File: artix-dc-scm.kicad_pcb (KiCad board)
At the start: 8 copper layers, 90 x 120.4 mm, 474 parts, among them IC1 TPS54561, IC2 TLV73312PDBVT, J1 L834-1G1T-S7, J12 S2B-PH-K-S_LF__SN_, J13 62000311121, J2 1-2199230-6, J3 543630489, J4 M20-7830642, J5 SFF-TA-1002-4C+, J6 0878311420, J7 61300611121, Q1 IRLML6402TRPBF, Q10 2N7002, Q11 2N7002, Q12 2N7002, Q13 2N7002, Q14 2N7002, Q15 2N7002, Q16 2N7002, Q2 IRLML6402TRPBF, Q3 IRLML6402TRPBF, Q4 IRLML6402TRPBF, Q5 IRLML6402TRPBF, Q6 IRLML6402TRPBF, Q7 2N7002, Q8 2N7002, Q9 2N7002, U1 MTFC16GAPALNA-AIT, U10 TPS62823DLCT, U11 TPS62823DLCT, U12 TPS62823DLCT, U13 TPS62823DLCT, U14 XC7A100T-FGG484, U15 SN74LVC1G08DCKR, U16 SN74LS08DBR, U17 USB3300-EZK-TR, U18 USB3300-EZK-TR, U2 W25Q32JVSSIQ_TR, U20 KSZ9031RNXCA, U3 W25Q32JVSSIQ_TR, U4 W25Q32JVSSIQ_TR, U5 W25Q32JVSSIQ_TR, U6 NVT2008DQ,115, U7 AS4C256M16D3, U8 TPS51200DRC, U9 LM3881MME_NOPB, Y1 TSX-3225, Y2 ABM8G-25.000MHZ-18-D2Y-T, Y3 TSX-3225

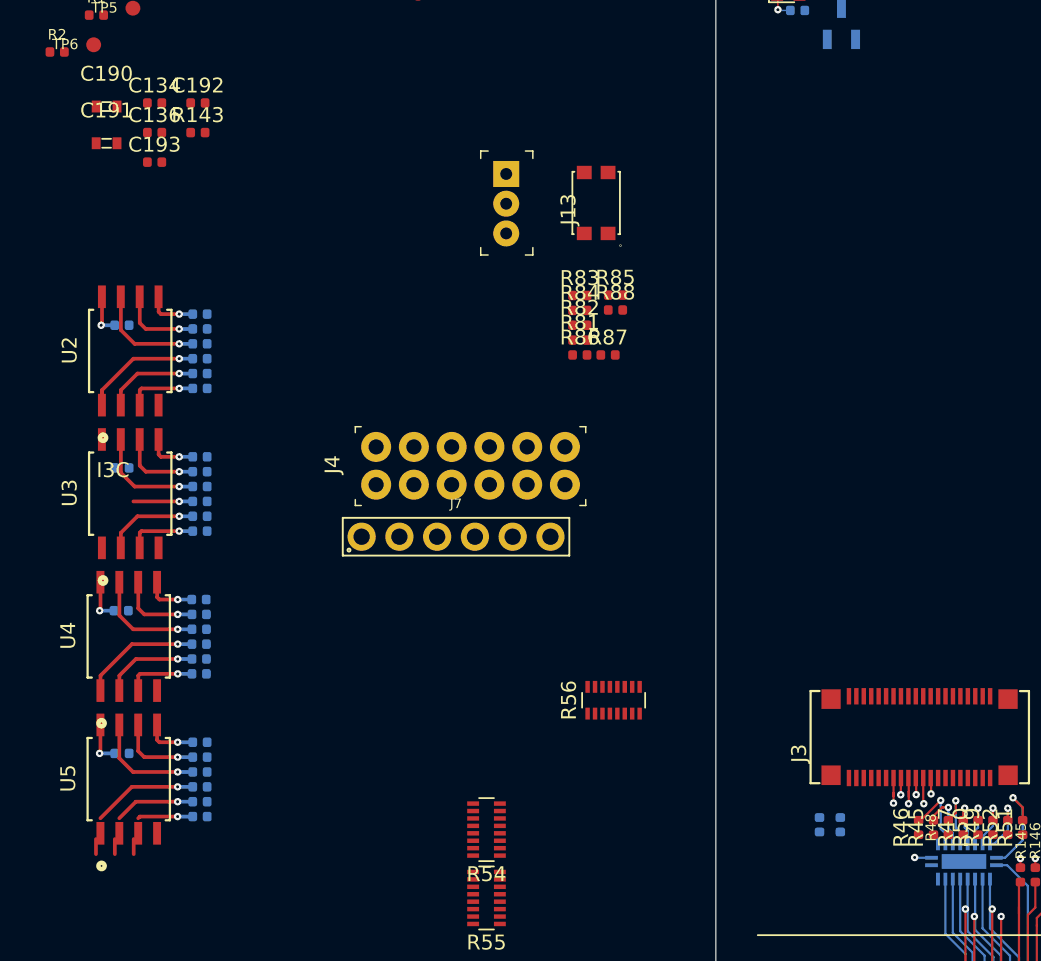
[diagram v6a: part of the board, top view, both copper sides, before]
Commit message: move Flash ICs under RoT
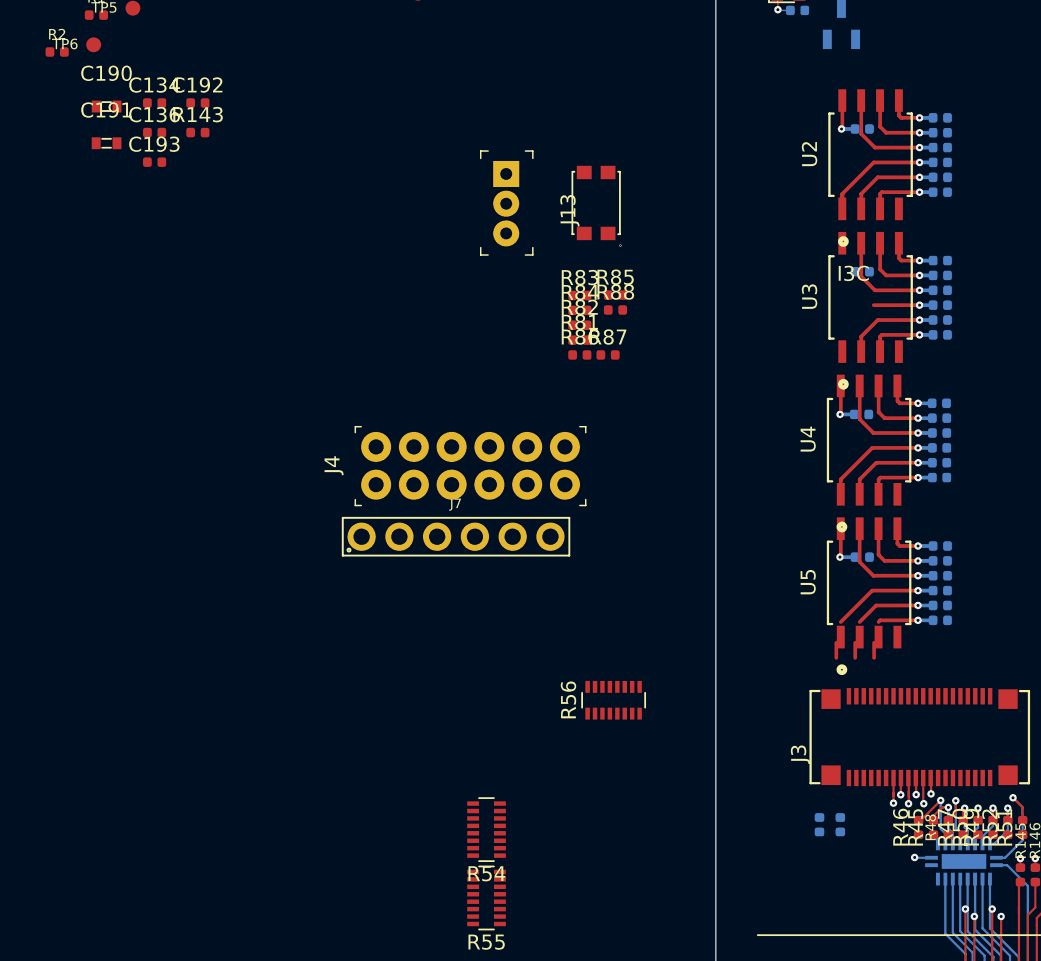
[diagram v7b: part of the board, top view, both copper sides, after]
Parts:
- moved C35 51.5 mm to (70.0, 115.1)
- moved C36 51.5 mm to (70.0, 124.7)
- moved R21 51.5 mm to (75.2, 117.3)
- moved R22 51.5 mm to (75.2, 126.9)
- moved R25 51.5 mm to (75.2, 115.3)
- moved R26 51.5 mm to (75.2, 124.9)
- moved R29 51.5 mm to (75.2, 114.3)
- moved R30 51.5 mm to (75.2, 123.9)
- moved R33 51.5 mm to (75.2, 119.3)
- moved R37 51.5 mm to (75.2, 116.3)
- moved R38 51.5 mm to (75.2, 125.9)
- moved R41 51.5 mm to (75.2, 118.3)
- moved R42 51.5 mm to (75.2, 127.9)
- moved U4 51.5 mm to (70.4, 136.0)
- moved U5 51.5 mm to (70.4, 145.6)
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
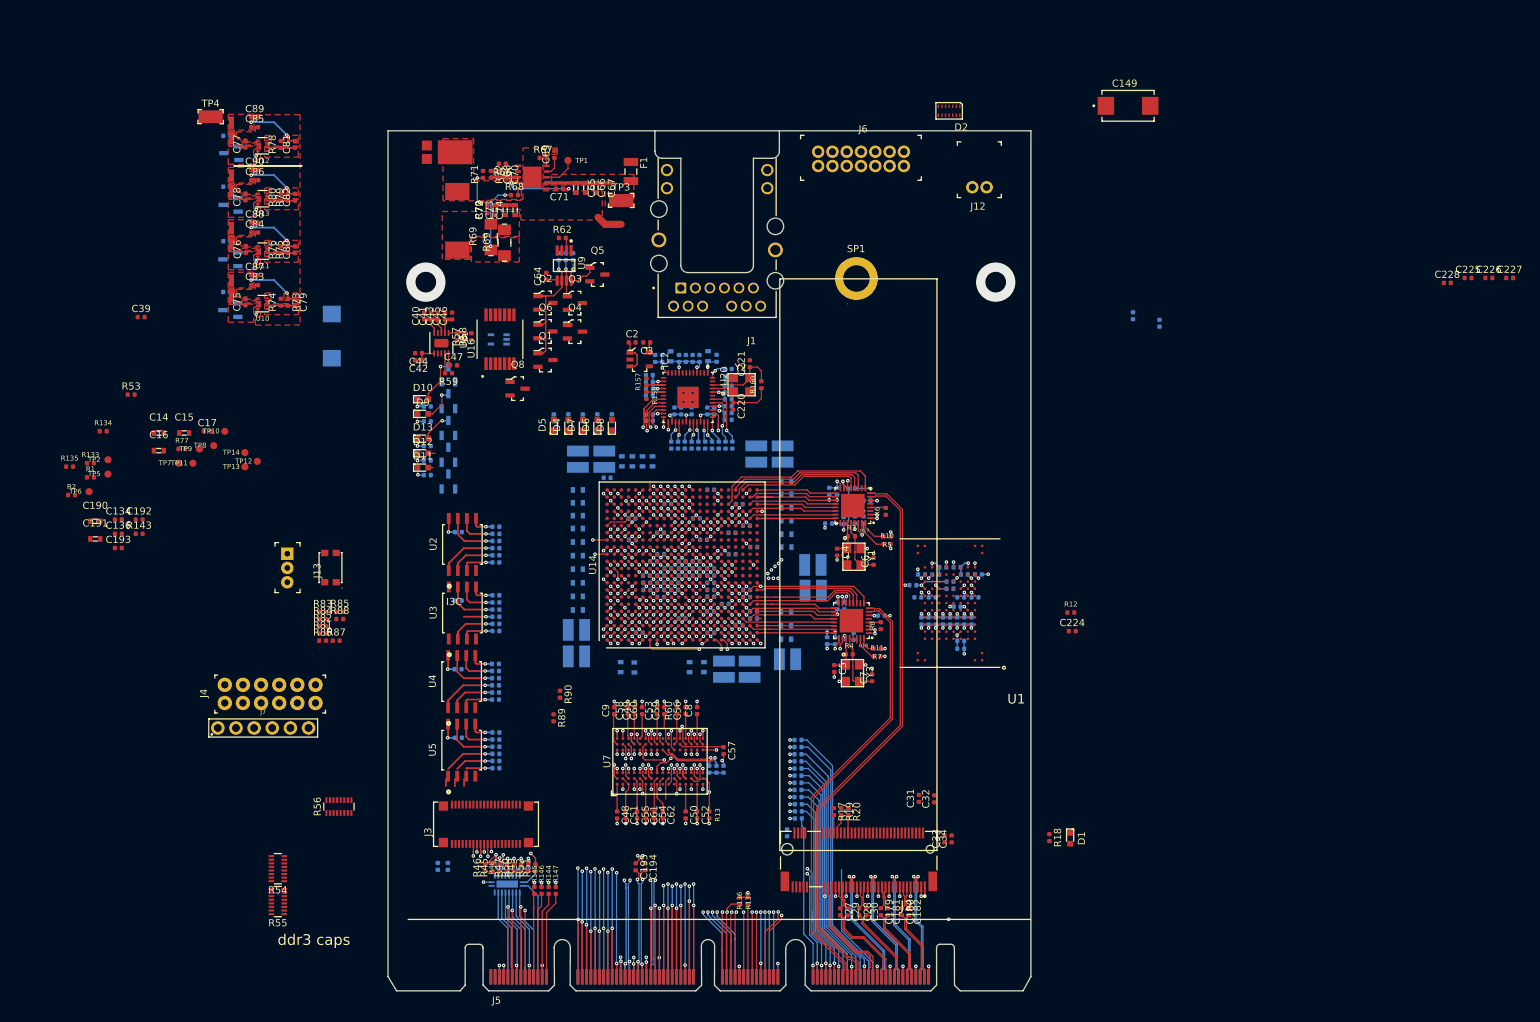
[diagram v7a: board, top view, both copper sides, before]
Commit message: Fix PCB outline
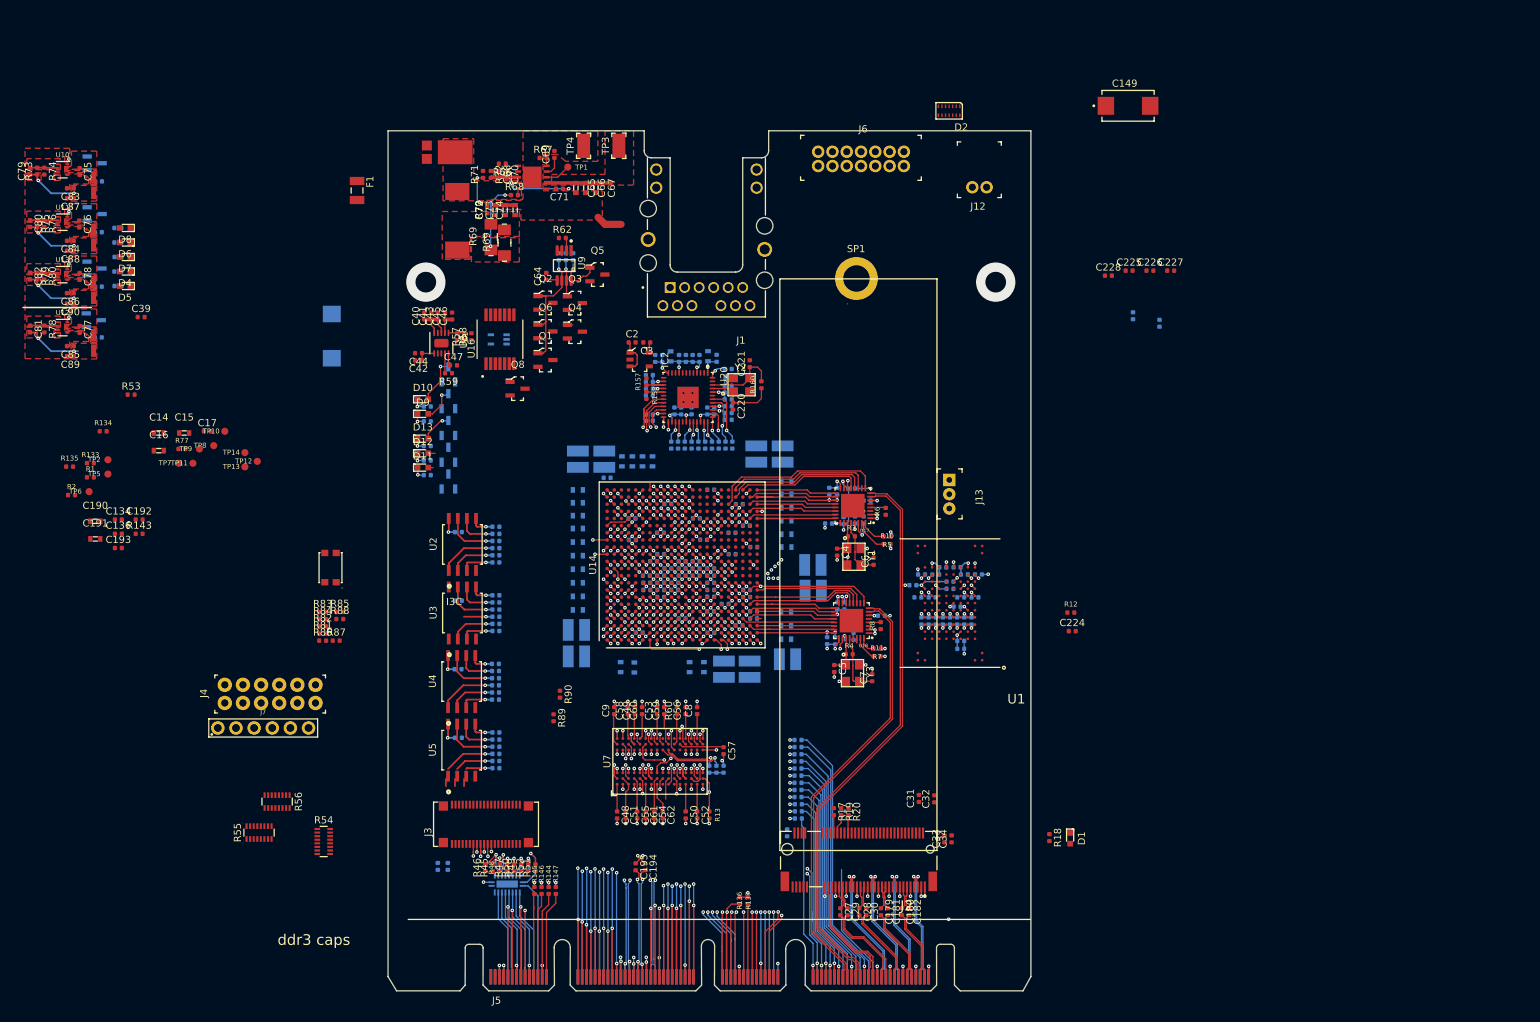
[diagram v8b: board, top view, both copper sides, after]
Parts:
- moved J13 93.2 mm to (138.7, 109.8)
- moved R98 74.1 mm to (22.3, 72.5), turned to 0 degrees
- moved D8 73.5 mm to (23.3, 72.5), turned to 180 degrees
- moved R96 71.5 mm to (22.3, 74.5), turned to 0 degrees
- moved D6 70.9 mm to (23.3, 74.5), turned to 180 degrees
- moved R97 68.9 mm to (22.3, 76.6), turned to 0 degrees
- moved D7 68.3 mm to (23.3, 76.6), turned to 180 degrees
- moved R94 66.3 mm to (22.3, 78.6), turned to 0 degrees
- moved D4 65.7 mm to (23.3, 78.6), turned to 180 degrees
- moved R95 63.7 mm to (22.3, 80.6), turned to 0 degrees
- moved D5 63.1 mm to (23.3, 80.6), turned to 180 degrees
- moved TP4 52.4 mm to (87.5, 61.0), turned to 90 degrees
- moved C225 47.5 mm to (163.8, 78.5)
- moved C226 47.5 mm to (166.8, 78.5)
- moved C227 47.5 mm to (169.7, 78.5)
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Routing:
- net Net-(IC1-Pad3): track 4.64 -> 3.57 mm
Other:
- outline, holes or cut-outs redrawn
